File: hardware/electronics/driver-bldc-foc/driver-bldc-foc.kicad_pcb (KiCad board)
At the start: 2 copper layers, 33 parts, among them J1 VBUS, J2 GND, J3 USB_A, J4 Motor_Phase_A, J5 Motor_Phase_B, J6 Motor_Phase_C, U1 TPS563240DDC, U2 STM32G473RETx, U3 AP1117-33, U4 DRV8353RSRGZT

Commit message: update pcb layout
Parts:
- added C13: 100nF, Capacitor_SMD:C_0805_2012Metric, F.Cu at (214.7, 257.9)
- added C14: 100nF, Capacitor_SMD:C_0805_2012Metric, F.Cu at (214.7, 260.9)
- added C15: 4.7uF, Capacitor_SMD:C_0805_2012Metric, F.Cu at (214.7, 263.9)
- added C16: 100nF, Capacitor_SMD:C_0805_2012Metric, F.Cu at (219.2, 257.9)
- added C17: 100nF, Capacitor_SMD:C_0805_2012Metric, F.Cu at (219.2, 260.9)
- added C18: 100nF, Capacitor_SMD:C_0805_2012Metric, F.Cu at (219.2, 263.9)
- added C19: 10nF, Capacitor_SMD:C_0805_2012Metric, F.Cu at (223.6, 257.9)
- added C20: 1uF, Capacitor_SMD:C_0805_2012Metric, F.Cu at (223.6, 260.9)
- added C21: 10nF, Capacitor_SMD:C_0805_2012Metric, F.Cu at (223.6, 263.9)
- added C22: 4.7uF, Capacitor_SMD:C_0805_2012Metric, F.Cu at (379.4, 199.0)
- added C23: 4.7uF, Capacitor_SMD:C_0805_2012Metric, F.Cu at (379.4, 202.0)
- added C24: 100nF, Capacitor_SMD:C_0805_2012Metric, F.Cu at (379.4, 205.0)
- added C25: 1uF, Capacitor_SMD:C_0805_2012Metric, F.Cu at (379.4, 208.0)
- added C26: 47nF, Capacitor_SMD:C_0805_2012Metric, F.Cu at (379.4, 211.0)
- added C27: 1uF, Capacitor_SMD:C_0805_2012Metric, F.Cu at (379.4, 214.1)
- added C28: 1uF, Capacitor_SMD:C_0805_2012Metric, F.Cu at (379.4, 217.1)
- added C29: 1uF, Capacitor_SMD:C_0805_2012Metric, F.Cu at (383.9, 199.0)
- added C30: 1uF, Capacitor_SMD:C_0805_2012Metric, F.Cu at (383.9, 202.0)
- added C31: 47nF, Capacitor_SMD:C_0805_2012Metric, F.Cu at (383.9, 205.0)
- added C32: 10nF, Capacitor_SMD:C_0805_2012Metric, F.Cu at (383.9, 208.0)
- added C33: 47nF, Capacitor_SMD:C_0805_2012Metric, F.Cu at (383.9, 211.0)
- added C34: 330p, Capacitor_SMD:C_0805_2012Metric, F.Cu at (383.9, 214.1)
- added C35: 4.7uF, Capacitor_SMD:C_0805_2012Metric, F.Cu at (383.9, 217.1)
- added C36: 4.7uF, Capacitor_SMD:C_0805_2012Metric, F.Cu at (388.3, 199.0)
- added C37: 2.2nF, Capacitor_SMD:C_0805_2012Metric, F.Cu at (388.3, 202.0)
- added C38: 2.2nF, Capacitor_SMD:C_0805_2012Metric, F.Cu at (388.3, 205.0)
- added C39: 2.2nF, Capacitor_SMD:C_0805_2012Metric, F.Cu at (388.3, 208.0)
- added C40: 1nF, Capacitor_SMD:C_0805_2012Metric, F.Cu at (388.3, 211.0)
- added C41: 1uF, Capacitor_SMD:C_0805_2012Metric, F.Cu at (388.3, 214.1)
- added C42: 1nF, Capacitor_SMD:C_0805_2012Metric, F.Cu at (388.3, 217.1)
- added C43: 1uF, Capacitor_SMD:C_0805_2012Metric, F.Cu at (392.8, 199.0)
- added C44: 1nF, Capacitor_SMD:C_0805_2012Metric, F.Cu at (392.8, 202.0)
- added C45: 1uF, Capacitor_SMD:C_0805_2012Metric, F.Cu at (392.8, 205.0)
- added D3: LED, LED_SMD:LED_0805_2012Metric, F.Cu at (229.2, 250.1)
- added D4: LED, LED_SMD:LED_0805_2012Metric, F.Cu at (229.2, 253.2)
- added D5: PMEG4005CEJ, Diode_SMD:D_SOD-323F, F.Cu at (397.2, 203.5)
- added D6: SS110, Diode_SMD:D_SMA, F.Cu at (399.1, 199.8)
- added D7: LED, LED_SMD:LED_0805_2012Metric, F.Cu at (238.2, 277.6)
- added FB1: FerriteBead_Small, Inductor_SMD:L_0201_0603Metric, F.Cu at (224.3, 266.3)
- added FB2: FerriteBead_Small, Inductor_SMD:L_0201_0603Metric, F.Cu at (224.3, 268.1)
- added J4: Motor_Phase_A, Connector_Wire:SolderWirePad_1x01_SMD_5x10mm, F.Cu at (215.8, 240.8)
- added J5: Motor_Phase_B, Connector_Wire:SolderWirePad_1x01_SMD_5x10mm, F.Cu at (222.4, 240.8)
- added J6: Motor_Phase_C, Connector_Wire:SolderWirePad_1x01_SMD_5x10mm, F.Cu at (229.0, 240.8)
- added J7: Conn_01x04_Pin, Connector_JST:JST_XH_B4B-XH-A_1x04_P2.50mm_Vertical, F.Cu at (216.0, 252.0)
- added JP1: SolderJumper_3_Open, Jumper:SolderJumper-3_P1.3mm_Open_RoundedPad1.0x1.5mm_NumberLabels, F.Cu at (215.3, 267.2)
- added Q1: BSC040N10NS5, Package_TO_SOT_SMD:TDSON-8-1, F.Cu at (237.5, 252.0)
- added Q2: BSC040N10NS5, Package_TO_SOT_SMD:TDSON-8-1, F.Cu at (373.1, 200.9)
- added Q3: BSC040N10NS5, Package_TO_SOT_SMD:TDSON-8-1, F.Cu at (373.1, 207.6)
- added Q4: BSC040N10NS5, Package_TO_SOT_SMD:TDSON-8-1, F.Cu at (373.1, 214.3)
- added Q5: BSC040N10NS5, Package_TO_SOT_SMD:TDSON-8-1, F.Cu at (373.1, 221.0)
- added Q6: BSC040N10NS5, Package_TO_SOT_SMD:TDSON-8-1, F.Cu at (373.1, 227.7)
- added R10: 470, Resistor_SMD:R_0805_2012Metric, F.Cu at (228.1, 266.7)
- added R11: 1k, Resistor_SMD:R_0805_2012Metric, F.Cu at (379.4, 220.0)
- added R12: 220k, Resistor_SMD:R_0805_2012Metric, F.Cu at (379.4, 223.0)
- added R13: 100k, Resistor_SMD:R_0805_2012Metric, F.Cu at (379.4, 225.9)
- added R14: 4k3, Resistor_SMD:R_0805_2012Metric, F.Cu at (379.4, 228.9)
- added R15: 3k9, Resistor_SMD:R_0805_2012Metric, F.Cu at (379.4, 231.8)
- added R16: 1k, Resistor_SMD:R_0805_2012Metric, F.Cu at (383.8, 220.0)
- added R17: 3k9, Resistor_SMD:R_0805_2012Metric, F.Cu at (383.8, 223.0)
- added R18: 22k, Resistor_SMD:R_0805_2012Metric, F.Cu at (383.8, 225.9)
- added R19: 1k, Resistor_SMD:R_0805_2012Metric, F.Cu at (383.8, 228.9)
- added R20: 22k, Resistor_SMD:R_0805_2012Metric, F.Cu at (383.8, 231.8)
- added R21: 1k, Resistor_SMD:R_0805_2012Metric, F.Cu at (388.2, 220.0)
- added R22: 22k, Resistor_SMD:R_0805_2012Metric, F.Cu at (388.2, 223.0)
- added R23: 1k, Resistor_SMD:R_0805_2012Metric, F.Cu at (388.2, 225.9)
- added R24: 2.5m, Resistor_SMD:R_2512_6332Metric, F.Cu at (394.8, 221.0)
- added R25: 2.5m, Resistor_SMD:R_2512_6332Metric, F.Cu at (394.8, 225.9)
- added R26: 2.5m, Resistor_SMD:R_2512_6332Metric, F.Cu at (394.8, 230.8)
- added R27: 470, Resistor_SMD:R_0805_2012Metric, F.Cu at (238.2, 280.6)
- added R7: 10K, Resistor_SMD:R_0805_2012Metric, F.Cu at (228.1, 257.9)
- added R8: 10K, Resistor_SMD:R_0805_2012Metric, F.Cu at (228.1, 260.8)
- added R9: 470, Resistor_SMD:R_0805_2012Metric, F.Cu at (228.1, 263.8)
- added TH1: Thermistor_NTC, Resistor_THT:R_Axial_DIN0204_L3.6mm_D1.6mm_P1.90mm_Vertical, F.Cu at (219.7, 267.0)
- added U5: ISO1042BDWVR, footprints:DWV0008A, F.Cu at (242.8, 270.5)
- C12: value 10uF -> 1nF
- L1: value L_Ferrite_Small -> 100uH
- R5: value 3k -> 100k
- R6: value 3k -> 3.9k
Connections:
- L1 pad 1: unconnected-(L1-Pad1) -> Net-(D6-K)
- L1 pad 2: unconnected-(L1-Pad2) -> /+12V
- U2 pad 1: unconnected-(U2-VBAT-Pad1) -> /MCU/3V3_MCU
- U2 pad 10: unconnected-(U2-PC2-Pad10) -> /VbusSense
- U2 pad 12: unconnected-(U2-PA0-Pad12) -> /MCU/FET_TEMP
- U2 pad 15: Net-(U2-VSS-Pad15) -> GND
- U2 pad 16: unconnected-(U2-VDD-Pad16) -> /MCU/3V3_MCU
- U2 pad 17: unconnected-(U2-PA3-Pad17) -> /MCU/VA
- U2 pad 19: unconnected-(U2-PA5-Pad19) -> /MCU/DRV_SCK
- U2 pad 2: unconnected-(U2-PC13-Pad2) -> /MCU/PWM_A-
- U2 pad 20: unconnected-(U2-PA6-Pad20) -> /MCU/DRV_MISO
- U2 pad 21: unconnected-(U2-PA7-Pad21) -> /MCU/IB
- U2 pad 22: unconnected-(U2-PC4-Pad22) -> /MCU/U1_TX
- U2 pad 23: unconnected-(U2-PC5-Pad23) -> /MCU/U1_RX
- U2 pad 24: unconnected-(U2-PB0-Pad24) -> /MCU/PWM_B-
- U2 pad 25: unconnected-(U2-PB1-Pad25) -> /MCU/IA
- U2 pad 27: unconnected-(U2-VSSA-Pad27) -> GND
- U2 pad 28: unconnected-(U2-VREF+-Pad28) -> /MCU/3V3_MCU_A
- U2 pad 29: unconnected-(U2-VDDA-Pad29) -> /MCU/3V3_MCU_A
- U2 pad 3: unconnected-(U2-PC14-Pad3) -> /MCU/LED1
- U2 pad 30: unconnected-(U2-PB10-Pad30) -> /MCU/OC
- U2 pad 31: Net-(U2-VSS-Pad15) -> GND
- U2 pad 32: unconnected-(U2-VDD-Pad32) -> /MCU/3V3_MCU
- U2 pad 34: unconnected-(U2-PB12-Pad34) -> /MCU/CAN_RX
- U2 pad 35: unconnected-(U2-PB13-Pad35) -> /MCU/CAN_TX
- U2 pad 36: unconnected-(U2-PB14-Pad36) -> /MCU/VB
- U2 pad 37: unconnected-(U2-PB15-Pad37) -> /MCU/PWM_C-
- U2 pad 38: unconnected-(U2-PC6-Pad38) -> /MCU/DVR_CS
- U2 pad 39: unconnected-(U2-PC7-Pad39) -> /MCU/DRV_EN
- U2 pad 4: unconnected-(U2-PC15-Pad4) -> /MCU/LED2
- U2 pad 40: unconnected-(U2-PC8-Pad40) -> /MCU/ENC_SCL
- U2 pad 41: unconnected-(U2-PC9-Pad41) -> /MCU/ENC_SDA
- U2 pad 42: unconnected-(U2-PA8-Pad42) -> /MCU/PWM_A+
- U2 pad 43: unconnected-(U2-PA9-Pad43) -> /MCU/PWM_B+
- U2 pad 44: unconnected-(U2-PA10-Pad44) -> /MCU/PWM_C+
- U2 pad 45: unconnected-(U2-PA11-Pad45) -> /MCU/USB_D-
- U2 pad 46: unconnected-(U2-PA12-Pad46) -> /MCU/USB_D+
- U2 pad 47: Net-(U2-VSS-Pad15) -> GND
- U2 pad 48: unconnected-(U2-VDD-Pad48) -> /MCU/3V3_MCU
- U2 pad 49: unconnected-(U2-PA13-Pad49) -> /MCU/DEBUG_DIO
- U2 pad 50: unconnected-(U2-PA14-Pad50) -> /MCU/DEBUG_CLK
- U2 pad 52: unconnected-(U2-PC10-Pad52) -> /MCU/ENC_SCK
- U2 pad 53: unconnected-(U2-PC11-Pad53) -> /MCU/ENC_MISO
- U2 pad 54: unconnected-(U2-PC12-Pad54) -> /MCU/ENC_MOSI
- U2 pad 58: unconnected-(U2-PB5-Pad58) -> /MCU/DRV_MOSI
- U2 pad 59: unconnected-(U2-PB6-Pad59) -> /MCU/ENC_EN
- U2 pad 60: unconnected-(U2-PB7-Pad60) -> /MCU/ENC_CS
- U2 pad 61: unconnected-(U2-PB8-Pad61) -> Net-(U2-PB8)
- U2 pad 63: Net-(U2-VSS-Pad15) -> GND
- U2 pad 64: unconnected-(U2-VDD-Pad64) -> /MCU/3V3_MCU
- U2 pad 8: unconnected-(U2-PC0-Pad8) -> /MCU/VC
- U2 pad 9: unconnected-(U2-PC1-Pad9) -> /MCU/IC
- U4 pad 1: unconnected-(U4-GND-Pad1) -> GND
- U4 pad 10: unconnected-(U4-GLA-Pad10) -> /ThreePhaseBridge and Power/GLA
- U4 pad 11: unconnected-(U4-SPA-Pad11) -> /ThreePhaseBridge and Power/SPA
- U4 pad 12: unconnected-(U4-SNA-Pad12) -> GND
- U4 pad 13: unconnected-(U4-SNB-Pad13) -> GND
- U4 pad 14: unconnected-(U4-SPB-Pad14) -> /ThreePhaseBridge and Power/SPB
- U4 pad 15: unconnected-(U4-GLB-Pad15) -> /ThreePhaseBridge and Power/GLB
- U4 pad 16: unconnected-(U4-SHB-Pad16) -> /ThreePhaseBridge and Power/SHB
- U4 pad 17: unconnected-(U4-GHB-Pad17) -> /ThreePhaseBridge and Power/GHB
- U4 pad 18: unconnected-(U4-GHC-Pad18) -> /ThreePhaseBridge and Power/GHC
- U4 pad 19: unconnected-(U4-SHC-Pad19) -> /ThreePhaseBridge and Power/SHC
- U4 pad 2: unconnected-(U4-VGLS-Pad2) -> Net-(U4-VGLS)
- U4 pad 20: unconnected-(U4-GLC-Pad20) -> /ThreePhaseBridge and Power/GLC
- U4 pad 21: unconnected-(U4-SPC-Pad21) -> /ThreePhaseBridge and Power/SPC
- U4 pad 22: unconnected-(U4-SNC-Pad22) -> GND
- U4 pad 23: unconnected-(U4-SOC-Pad23) -> /MCU/IC
- U4 pad 24: unconnected-(U4-SOB-Pad24) -> /MCU/IB
- U4 pad 25: unconnected-(U4-SOA-Pad25) -> /MCU/IA
- U4 pad 26: unconnected-(U4-VREF-Pad26) -> +3.3V
- U4 pad 27: unconnected-(U4-AGND-Pad27) -> GND
- U4 pad 28: unconnected-(U4-~{FAULT}-Pad28) -> /MCU/OC
- U4 pad 29: unconnected-(U4-SDO-Pad29) -> /MCU/DRV_MOSI
- U4 pad 3: unconnected-(U4-CPL-Pad3) -> Net-(U4-CPL)
- U4 pad 30: unconnected-(U4-SDI-Pad30) -> /MCU/DRV_MISO
- U4 pad 31: unconnected-(U4-SCLK-Pad31) -> /MCU/DRV_SCK
- U4 pad 32: unconnected-(U4-~{SCS}-Pad32) -> /MCU/DVR_CS
- U4 pad 33: unconnected-(U4-ENABLE-Pad33) -> /MCU/DRV_EN
- U4 pad 34: unconnected-(U4-INHA-Pad34) -> /MCU/PWM_A+
- U4 pad 35: unconnected-(U4-INLA-Pad35) -> /MCU/PWM_A-
- U4 pad 36: unconnected-(U4-INHB-Pad36) -> /MCU/PWM_B+
- U4 pad 37: unconnected-(U4-INLB-Pad37) -> /MCU/PWM_B-
- U4 pad 38: unconnected-(U4-INHC-Pad38) -> /MCU/PWM_C+
- U4 pad 39: unconnected-(U4-INLC-Pad39) -> /MCU/PWM_C-
- U4 pad 4: unconnected-(U4-CPH-Pad4) -> Net-(U4-CPH)
- U4 pad 40: unconnected-(U4-DVDD-Pad40) -> Net-(U4-DVDD)
- U4 pad 41: unconnected-(U4-DGND-Pad41) -> GND
- U4 pad 42: unconnected-(U4-SW-Pad42) -> Net-(D6-K)
- U4 pad 43: unconnected-(U4-VIN-Pad43) -> VBUS
- U4 pad 44: unconnected-(U4-VCC-Pad44) -> /ThreePhaseBridge and Power/BUCKVCC
- U4 pad 45: unconnected-(U4-BST-Pad45) -> Net-(U4-BST)
- U4 pad 46: unconnected-(U4-RCL-Pad46) -> Net-(U4-RCL)
- U4 pad 47: unconnected-(U4-RT/SD-Pad47) -> Net-(U4-RT/SD)
- U4 pad 48: unconnected-(U4-FB-Pad48) -> Net-(U4-FB)
- U4 pad 49: unconnected-(U4-EXP-Pad49) -> GND
- U4 pad 5: unconnected-(U4-VM-Pad5) -> VBUS
- U4 pad 6: unconnected-(U4-VDRAIN-Pad6) -> VBUS
- U4 pad 7: unconnected-(U4-VCP-Pad7) -> Net-(U4-VCP)
- U4 pad 8: unconnected-(U4-GHA-Pad8) -> /ThreePhaseBridge and Power/GHA
- U4 pad 9: unconnected-(U4-SHA-Pad9) -> /ThreePhaseBridge and Power/SHA

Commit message: fix pcb
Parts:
- added J8: XT30PW-M, XT30PW-M:AMASS_XT30PW-M, F.Cu at (320.9, 264.4)
- added U5: TJA1051T-3, Package_SO:SOIC-8_3.9x4.9mm_P1.27mm, F.Cu at (332.5, 264.0)
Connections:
- net /MCU/DVR_CS renamed /MCU/DRV_CS
- net /MCU/USB_D+ renamed /USB_D+
- net /MCU/USB_D- renamed /USB_D-
- U2 pad 34: /MCU/CAN_RX -> /CAN_RX
- U2 pad 35: /MCU/CAN_TX -> /CAN_TX

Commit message: route power tracks
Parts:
- removed C1: 10uF, Capacitor_SMD:C_0805_2012Metric
- removed C2: 1uF, Capacitor_SMD:C_0805_2012Metric
- removed C3, C4: 100nF, Capacitor_SMD:C_0805_2012Metric
- removed the J1 at (344.8, 199.4)
- removed the J4 at (297.8, 224.8)
- removed the J5 at (304.4, 224.8)
- removed the J6 at (311.0, 224.8)
- removed J8: XT30PW-M, XT30PW-M:AMASS_XT30PW-M
- removed L2: 1.5uH, Inductor_SMD:L_APV_ANR5040
- removed R1: 3k, Resistor_SMD:R_0805_2012Metric
- removed R2: 22k, Resistor_SMD:R_0805_2012Metric
- removed the U5 at (242.8, 270.5)
- added J1: Conn_01x03_Pin, Connector_Wire:SolderWire-0.127sqmm_1x03_P3.7mm_D0.48mm_OD1mm, F.Cu at (208.9, 70.4)
- added J1: Conn_01x01_Pin, Connector_Wire:SolderWirePad_1x01_SMD_2x4mm, F.Cu at (134.2, 102.4)
- added J10: Conn_01x01_Pin, Connector_Wire:SolderWirePad_1x01_SMD_2x4mm, F.Cu at (223.0, 132.7)
- added J11: Conn_01x01_Pin, Connector_Wire:SolderWirePad_1x01_SMD_2x4mm, F.Cu at (226.6, 132.7)
- added J12: Conn_01x01_Pin, Connector_Wire:SolderWirePad_1x01_SMD_2x4mm, F.Cu at (137.9, 157.7)
- added J13: Conn_01x01_Pin, Connector_Wire:SolderWirePad_1x01_SMD_2x4mm, F.Cu at (140.7, 157.7)
- added J14: Conn_01x01_Pin, Connector_Wire:SolderWirePad_1x01_SMD_2x4mm, F.Cu at (143.5, 157.7)
- added J15: Conn_01x01_Pin, Connector_Wire:SolderWirePad_1x01_SMD_2x4mm, F.Cu at (226.5, 126.4)
- added J16: Conn_01x01_Pin, Connector_Wire:SolderWirePad_1x01_SMD_2x4mm, F.Cu at (146.3, 157.7)
- added J17: Conn_01x01_Pin, Connector_Wire:SolderWirePad_1x01_SMD_2x4mm, F.Cu at (226.6, 138.3)
- added J18: Conn_01x01_Pin, Connector_Wire:SolderWirePad_1x01_SMD_2x4mm, F.Cu at (230.1, 138.3)
- added J19: Conn_01x01_Pin, Connector_Wire:SolderWirePad_1x01_SMD_2x4mm, F.Cu at (139.8, 102.4)
- added J20: Conn_01x01_Pin, Connector_Wire:SolderWirePad_1x01_SMD_2x4mm, F.Cu at (135.1, 157.7)
- added J21: Conn_01x01_Pin, Connector_Wire:SolderWirePad_1x01_SMD_2x4mm, F.Cu at (219.5, 143.8)
- added J22: Conn_01x01_Pin, Connector_Wire:SolderWirePad_1x01_SMD_2x4mm, F.Cu at (223.0, 143.8)
- added J9: Conn_01x01_Pin, Connector_Wire:SolderWirePad_1x01_SMD_2x4mm, F.Cu at (149.1, 157.7)
- added R28: 5.1k, Resistor_SMD:R_0805_2012Metric, F.Cu at (230.5, 148.1)
- added R29: 5.1k, Resistor_SMD:R_0805_2012Metric, F.Cu at (230.5, 151.0)
- added U6: XT30PW-M, XT30PWM:XT30PW-M_AMA, F.Cu at (127.0, 112.4)
- C22, C23, C25: footprint Capacitor_SMD:C_0805_2012Metric -> Capacitor_SMD:C_1210_3225Metric
- C41, C43, C45: footprint Capacitor_SMD:C_0805_2012Metric -> Capacitor_SMD:C_1206_3216Metric
- J2: value GND -> Conn_01x01_Pin; footprint Connector_Wire:SolderWirePad_1x01_SMD_5x10mm -> Connector_Wire:SolderWirePad_1x01_SMD_2x4mm
- J3: value USB_A -> KH-TYPE-C-16P; footprint Connector_USB:USB_B_OST_USB-B1HSxx_Horizontal -> KH-TYPE-C-16P:KINGHELM_KH-TYPE-C-16P
- moved R24 282.4 mm to (130.0, 122.9), turned to 180 degrees
- moved C43 280.4 mm to (124.7, 116.9), turned to 180 degrees
- moved R25 279.4 mm to (130.0, 136.9), turned to 180 degrees
- moved C41 276.8 mm to (124.6, 130.1), turned to 180 degrees
- moved R26 276.5 mm to (130.0, 151.4), turned to 180 degrees
- moved C45 275.0 mm to (124.6, 144.1), turned to 180 degrees
- moved D6 274.1 mm to (130.7, 144.2), turned to 180 degrees
- moved Q4 272.0 mm to (114.5, 129.8), turned to 180 degrees
- moved Q2 272.0 mm to (114.5, 116.7), turned to 180 degrees
- moved Q6 271.9 mm to (114.5, 143.8), turned to 180 degrees
- moved Q3 268.2 mm to (114.5, 136.6)
- moved Q5 267.9 mm to (114.5, 150.8)
- moved D5 265.0 mm to (139.6, 141.1), turned to -90 degrees
- moved R21 262.9 mm to (130.9, 166.3), turned to 90 degrees
- moved R22 261.1 mm to (138.4, 147.1), turned to 180 degrees
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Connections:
- D1 pad 2: /USB_VBUS -> VBUS
- J2 pad 1: GND -> Net-(J2-Pin_1)
- U2 pad 51: unconnected-(U2-PA15-Pad51) -> /MCU/TIM2_CH1
- U5 pad 6: unconnected-(U5-CANL-Pad6) -> Net-(J2-Pin_1)
- U5 pad 7: unconnected-(U5-CANH-Pad7) -> Net-(J1-Pin_1)
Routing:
- net /ThreePhaseBridge and Power/GHC: track 0.00 -> 54.4 mm, vias 0 -> 2
- net /ThreePhaseBridge and Power/GHB: track 0.00 -> 41.5 mm, vias 0 -> 2
- net /ThreePhaseBridge and Power/GLA: track 0.00 -> 39.1 mm, vias 0 -> 2
- net /ThreePhaseBridge and Power/GHA: track 0.00 -> 39.1 mm, vias 0 -> 2
- net Net-(D6-K): track 0.00 -> 36.5 mm
- net /ThreePhaseBridge and Power/GLC: track 0.00 -> 34.8 mm, vias 0 -> 2
- net /ThreePhaseBridge and Power/GLB: track 0.00 -> 26.5 mm, vias 0 -> 2
- net /ThreePhaseBridge and Power/BUCKVCC: track 0.00 -> 24.7 mm, vias 0 -> 2
- net VBUS: track 0.00 -> 24.5 mm, vias 0 -> 25
- net GND: track 0.00 -> 19.4 mm, vias 0 -> 97
- net /+12V: track 0.00 -> 13.2 mm
- net Net-(U4-BST): track 0.00 -> 12.6 mm, vias 0 -> 2
- net Net-(U4-FB): track 0.00 -> 11.7 mm
- net /VbusSense: track 0.00 -> 10.2 mm
- net Net-(U4-RT/SD): track 0.00 -> 6.87 mm
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- added copper zone on F.Cu, net /ThreePhaseBridge and Power/SHA
- added copper zone on F.Cu, net /ThreePhaseBridge and Power/SHB
- added copper zone on F.Cu, net /ThreePhaseBridge and Power/SHC
- added copper zone on B.Cu, net /ThreePhaseBridge and Power/SPA
- added copper zone on F.Cu, net /ThreePhaseBridge and Power/SPA
- added copper zone on B.Cu, net /ThreePhaseBridge and Power/SPB
- added copper zone on F.Cu, net /ThreePhaseBridge and Power/SPB
- added copper zone on B.Cu, net /ThreePhaseBridge and Power/SPC
- added copper zone on F.Cu, net /ThreePhaseBridge and Power/SPC
- added copper zone on F.Cu, net GND
- added copper zone on In1.Cu, net GND
- added copper zone on B.Cu, net VBUS
- added copper zone on F.Cu, net VBUS
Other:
- board outline added: 80 x 60 mm
- copper layers 2 -> 4

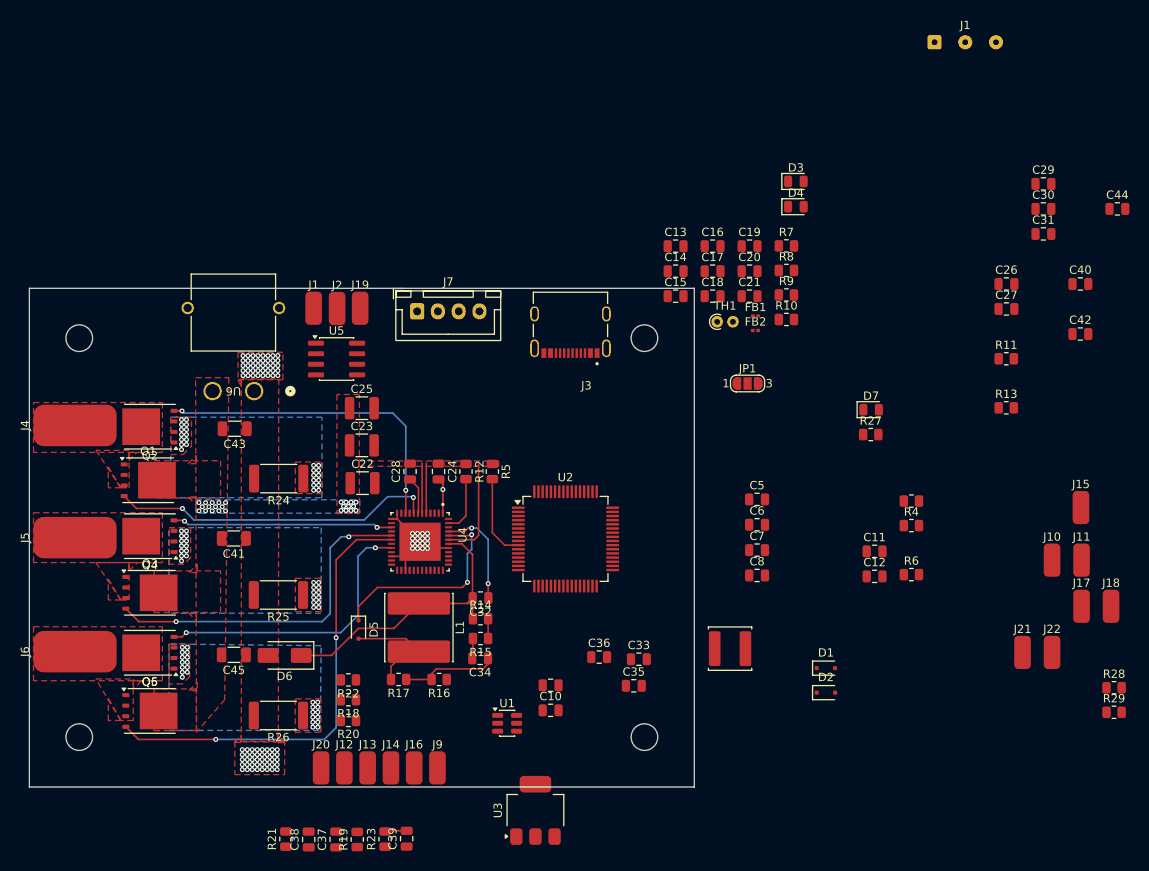
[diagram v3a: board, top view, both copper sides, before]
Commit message: Update driver-bldc-foc schematics, PCB layout, and DRC reports
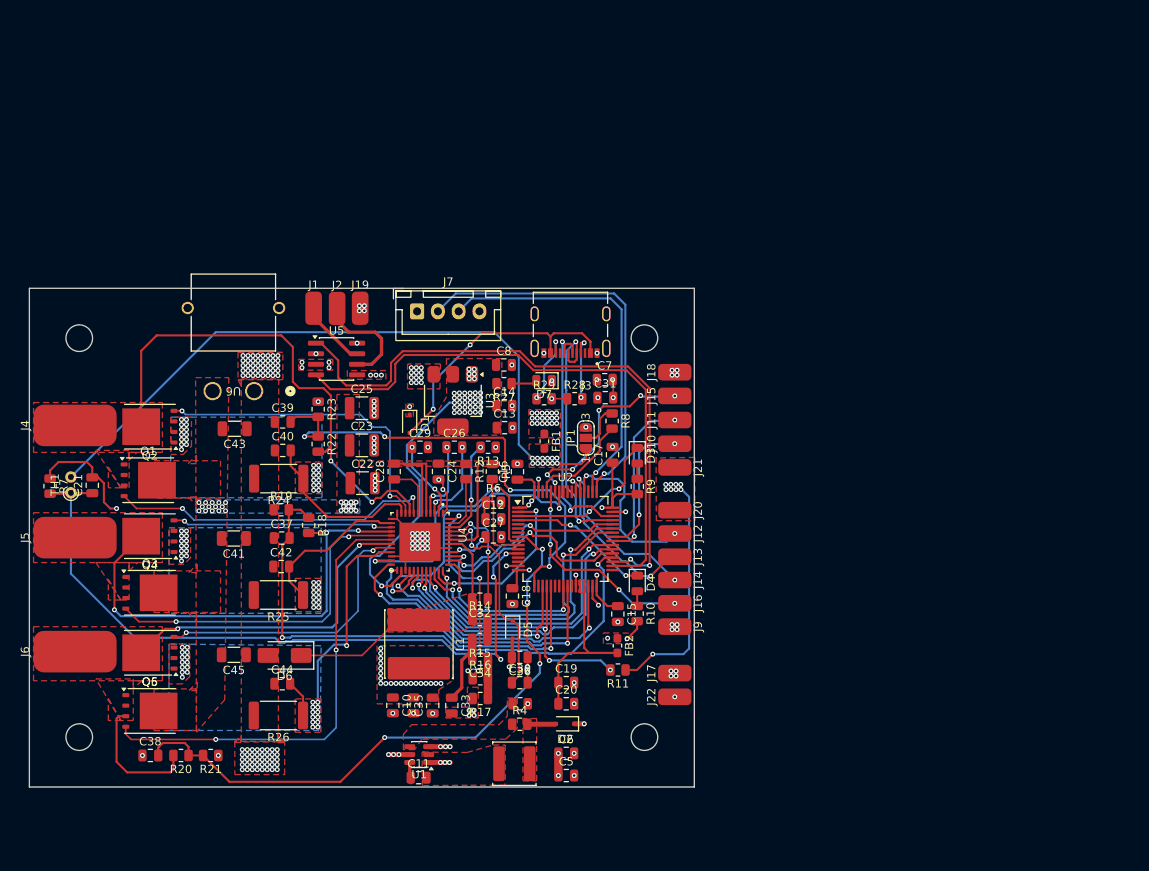
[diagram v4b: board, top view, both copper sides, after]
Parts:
- removed the J1 at (208.9, 70.4)
- FB1, FB2: footprint Inductor_SMD:L_0201_0603Metric -> Inductor_SMD:L_0603_1608Metric_Pad1.05x0.95mm_HandSolder
- moved C44 115.6 mm to (130.4, 147.6)
- moved C42 100.1 mm to (130.3, 133.5)
- moved C40 98.0 mm to (130.5, 119.5)
- moved R7 93.2 mm to (102.5, 123.8), turned to -90 degrees
- moved C30 85.0 mm to (159.0, 147.4)
- moved C21 82.3 mm to (107.6, 123.7), turned to 90 degrees
- moved C29 81.4 mm to (147.0, 119.1)
- moved TH1 80.4 mm to (105.0, 124.6), turned to 90 degrees
- moved R29 78.3 mm to (161.9, 113.3)
- moved R28 73.6 mm to (165.6, 113.3)
- moved C26 69.3 mm to (151.1, 119.1)
- moved C27 67.5 mm to (155.8, 129.9)
- moved R13 62.5 mm to (155.2, 119.1), turned to 180 degrees
- moved C11 61.2 mm to (146.8, 158.9)
- moved R11 59.9 mm to (170.8, 145.9), turned to 180 degrees
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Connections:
- D1 pad 2: VBUS -> V
- J3 pad A4B9: VBUS -> V
- J3 pad A9B4: VBUS -> V
- J7 pad 1: /MCU/3V3_MCU -> +3.3V
- R27 pad 2: /MCU/3V3_MCU -> +3.3V
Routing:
- net /MCU/3V3_MCU: track 0.00 -> 109.7 mm, vias 0 -> 19
- net /MCU/FET_TEMP: track 0.00 -> 86.3 mm, vias 0 -> 3
- net /MCU/VC: track 0.00 -> 74.9 mm, vias 0 -> 4
- net /CAN_TX: track 0.00 -> 74.5 mm, vias 0 -> 2
- net /CAN_RX: track 0.00 -> 69.9 mm
- net /MCU/VB: track 0.00 -> 69.0 mm, vias 0 -> 2
- net /ThreePhaseBridge and Power/SHA: track 4.39 -> 66.1 mm, vias 0 -> 2
- net +3.3V: track 0.00 -> 61.3 mm, vias 0 -> 63
- net /ThreePhaseBridge and Power/SHB: track 0.00 -> 55.8 mm, vias 0 -> 3
- net /MCU/VA: track 2.63 -> 57.8 mm, vias 0 -> 4
- net /ThreePhaseBridge and Power/SHC: track 0.00 -> 55.0 mm, vias 0 -> 2
- net /MCU/DEBUG_DIO: track 0.00 -> 48.2 mm, vias 0 -> 1
- net /MCU/DEBUG_CLK: track 0.00 -> 44.2 mm, vias 0 -> 1
- net /MCU/DRV_MISO: track 0.00 -> 39.2 mm, vias 0 -> 4
- net /MCU/DRV_MOSI: track 0.00 -> 35.9 mm, vias 0 -> 2
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- added copper zone on F.Cu, net +3.3V
- added copper zone on In2.Cu, net +3.3V
- added copper zone on F.Cu, net +5V
- added copper zone on In2.Cu, net +5V
- added copper zone on F.Cu, net /+12V
- added copper zone on In2.Cu, net /+12V
- added copper zone on F.Cu, net /5V_BUCK
- added copper zone on F.Cu, net /MCU/3V3_MCU
- added copper zone on In2.Cu, net /MCU/3V3_MCU
- added copper zone on F.Cu, net /MCU/3V3_MCU_A
- added copper zone on F.Cu, net Net-(D6-K)
- added copper zone on F.Cu, net Net-(U1-SW)
- added copper zone on F.Cu, net Net-(U1-VFB)
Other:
- rule pad_to_mask_clearance: 0 -> -0.03
